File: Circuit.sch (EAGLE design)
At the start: 120 parts, among them IC1 LM1117T-3.3-V, U1 MAG3110, U10 MMA8452Q, U11 MMA8452Q, U12 MMA8452Q, U2 MAG3110, U3 L3G4200D, U4 L3G4200D, U5 L3G4200D, U6 L3G4200D, U7 MMA8452Q, U8 MMA8452Q, U9 MMA8452Q

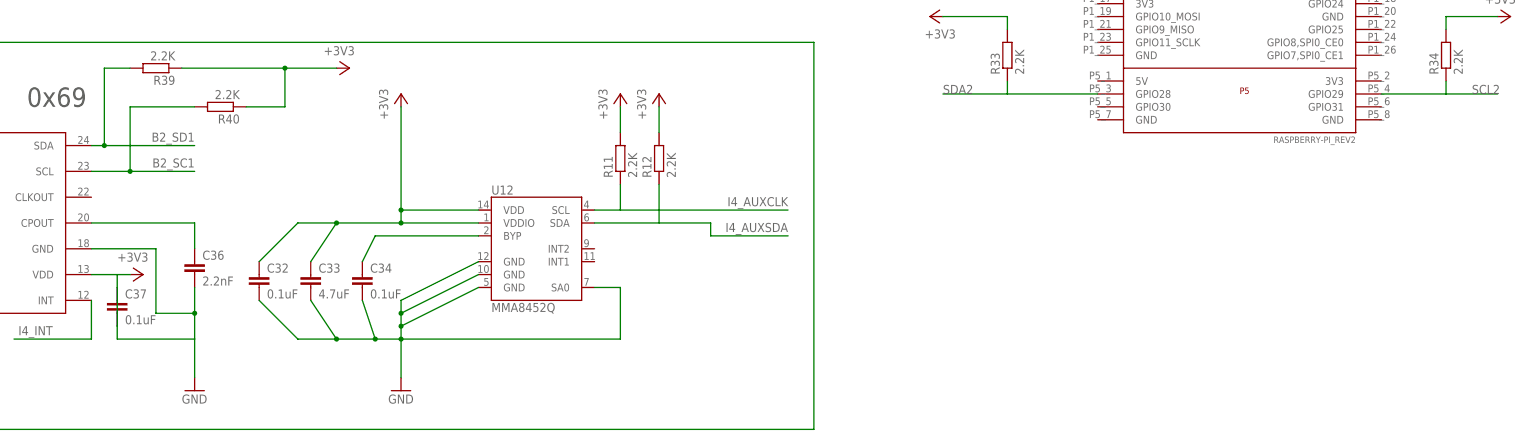
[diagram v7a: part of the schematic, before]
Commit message: Changes to raspi headers
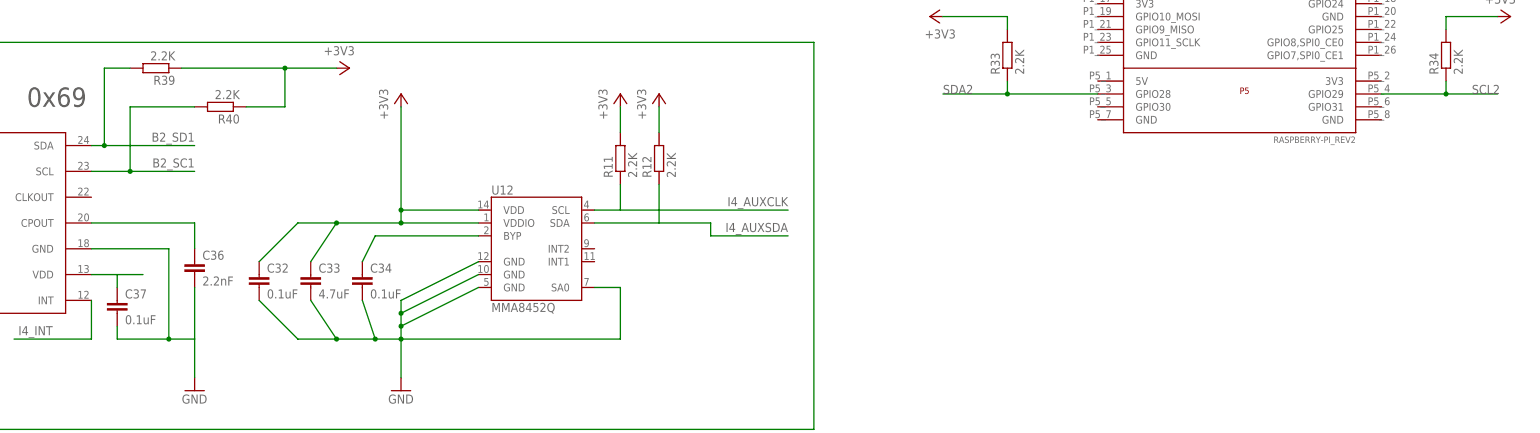
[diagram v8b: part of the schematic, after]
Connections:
- new net N$22: ITG4.VDD
- new net N$24: C37.1
- net +3V3: no longer C36.2, C37.1, C37.2, ITG4.GND, ITG4.VDD
- net GND: now also C36.2, C37.2, ITG4.GND
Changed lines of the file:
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@@
 <part name="C36" library="SparkFun" deviceset="CAP" device="0402-CAP" value="2.2nF"/>
 <part name="GND25" library="supply1" deviceset="GND" device=""/>
-<part name="+3V31" library="supply1" deviceset="+3V3" device=""/>
 <part name="C37" library="SparkFun" deviceset="CAP" device="0402-CAP" value="0.1uF"/>
 <part name="C38" library="SparkFun" deviceset="CAP" device="0402-CAP" value="10nF"/>
@@
 <instance part="C36" gate="G$1" x="215.9" y="119.38"/>
 <instance part="GND25" gate="1" x="215.9" y="96.52"/>
-<instance part="+3V31" gate="G$1" x="205.74" y="119.38" rot="R270"/>
 <instance part="C37" gate="G$1" x="200.66" y="111.76"/>
 <instance part="C38" gate="G$1" x="139.7" y="111.76"/>
@@
 <pinref part="GND39" gate="1" pin="GND"/>
 </segment>
+<segment>
+<pinref part="C37" gate="G$1" pin="2"/>
+<wire x1="200.66" y1="109.22" x2="200.66" y2="106.68" width="0.1524" layer="91"/>
+<pinref part="C36" gate="G$1" pin="2"/>
+<pinref part="GND25" gate="1" pin="GND"/>
+<wire x1="215.9" y1="116.84" x2="215.9" y2="106.68" width="0.1524" layer="91"/>
+<wire x1="215.9" y1="106.68" x2="215.9" y2="99.06" width="0.1524" layer="91"/>
+<wire x1="200.66" y1="106.68" x2="210.82" y2="106.68" width="0.1524" layer="91"/>
+<pinref part="ITG4" gate="G$1" pin="GND"/>
+<wire x1="210.82" y1="106.68" x2="215.9" y2="106.68" width="0.1524" layer="91"/>
+<wire x1="195.58" y1="124.46" x2="210.82" y2="124.46" width="0.1524" layer="91"/>
+<wire x1="210.82" y1="124.46" x2="210.82" y2="106.68" width="0.1524" layer="91"/>
+<junction x="210.82" y="106.68"/>
+</segment>
 </net>
 <net name="CLK1" class="0">
@@
 <wire x1="375.92" y1="154.94" x2="363.22" y2="154.94" width="0.1524" layer="91"/>
 <wire x1="375.92" y1="154.94" x2="375.92" y2="157.48" width="0.1524" layer="91"/>
+<junction x="375.92" y="154.94"/>
 </segment>
 <segment>
@@
 <wire x1="462.28" y1="154.94" x2="472.44" y2="154.94" width="0.1524" layer="91"/>
 <wire x1="462.28" y1="154.94" x2="462.28" y2="157.48" width="0.1524" layer="91"/>
+<junction x="462.28" y="154.94"/>
 </segment>
 </net>
@@
 </segment>
 <segment>
-<pinref part="ITG4" gate="G$1" pin="VDD"/>
-<wire x1="195.58" y1="119.38" x2="200.66" y2="119.38" width="0.1524" layer="91"/>
-<pinref part="+3V31" gate="G$1" pin="+3V3"/>
-<pinref part="C37" gate="G$1" pin="1"/>
-<wire x1="200.66" y1="119.38" x2="203.2" y2="119.38" width="0.1524" layer="91"/>
-<wire x1="200.66" y1="119.38" x2="200.66" y2="116.84" width="0.1524" layer="91"/>
-<pinref part="C37" gate="G$1" pin="2"/>
-<wire x1="200.66" y1="116.84" x2="200.66" y2="109.22" width="0.1524" layer="91"/>
-<wire x1="200.66" y1="109.22" x2="200.66" y2="106.68" width="0.1524" layer="91"/>
-<pinref part="C36" gate="G$1" pin="2"/>
-<wire x1="215.9" y1="116.84" x2="215.9" y2="111.76" width="0.1524" layer="91"/>
-<pinref part="GND25" gate="1" pin="GND"/>
-<pinref part="ITG4" gate="G$1" pin="GND"/>
-<wire x1="215.9" y1="111.76" x2="215.9" y2="106.68" width="0.1524" layer="91"/>
-<wire x1="215.9" y1="106.68" x2="215.9" y2="99.06" width="0.1524" layer="91"/>
-<wire x1="195.58" y1="124.46" x2="208.28" y2="124.46" width="0.1524" layer="91"/>
-<wire x1="208.28" y1="124.46" x2="208.28" y2="111.76" width="0.1524" layer="91"/>
-<wire x1="208.28" y1="111.76" x2="215.9" y2="111.76" width="0.1524" layer="91"/>
-<junction x="215.9" y="111.76"/>
-<wire x1="200.66" y1="106.68" x2="215.9" y2="106.68" width="0.1524" layer="91"/>
-</segment>
-<segment>
 <pinref part="ITG4" gate="G$1" pin="VLOGIC"/>
 <pinref part="+3V30" gate="G$1" pin="+3V3"/>
@@
 </segment>
 </net>
+<net name="N$22" class="0">
+<segment>
+<pinref part="ITG4" gate="G$1" pin="VDD"/>
+<wire x1="195.58" y1="119.38" x2="205.74" y2="119.38" width="0.1524" layer="91"/>
+</segment>
+</net>
+<net name="N$24" class="0">
+<segment>
+<pinref part="C37" gate="G$1" pin="1"/>
+<wire x1="200.66" y1="119.38" x2="200.66" y2="116.84" width="0.1524" layer="91"/>
+</segment>
+</net>
 </nets>
 </sheet>
 </sheets>
-<errors>
-</errors>
 </schematic>
 </drawing>
